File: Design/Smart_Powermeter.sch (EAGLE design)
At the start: 66 parts, among them IC1 AMS1117-3.3, IC3 ESP32-S2-MINI-1-N4R2, J1 AUDIO_JACK_TRRSSMD_RA, J2 AUDIO_JACK_TRRSSMD_RA, J3 AUDIO_JACK_TRRSSMD_RA, J4 AUDIO_JACK_TRRSSMD_RA, J5 AUDIO_JACK_TRRSSMD_RA, J6 AUDIO_JACK_TRRSSMD_RA, J8 USB-C, Q1 IRLML0100

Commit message: First draft for the Pro version
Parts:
- removed X1: (no value), con-wago-508:W237-02P
- added C16, C20, C21: 10u/6V, rcl:C-USC0603
- added D4, D5, D7: ESD5Z3.3T1G, microbuilder:DIODESOD-523
- added F1, F2, F3: 1A x 250V, OpenEnergyMonitor:FUSE
- added JP1, JP2, JP3, JP4, JP5, JP6: JUMPER-SMT_2_NC_TRACE_NO-SILK, SparkFun-Jumpers:JUMPER-SMT_2_NC_TRACE_NO-SILK
- added M1, M2, M3: 275VAC, OpenEnergyMonitor:MOV_14MM_275VAC
- added R21, R22, R23, R24, R26, R27, R28, R32, R33, R34, R35, R38, R39, R40, R48, R49, R50, R51, R52, R53, R54: 10k, rcl:R-US_R0603
- added R29, R41, R55: 180k, rcl:R-US_R0603
- added R30, R42, R56: 33k, rcl:R-US_R0603
- added R31, R43, R57: 1k, rcl:R-US_R0603
- added T1, T2, T3: ZMPT101B, OpenEnergyMonitor:ZMPT101B
- added X2: (no value), con-wago-508:W237-05P
- J1, J2, J3, J4, J5, J6: value AUDIO_JACK_TRRSSMD_RA -> AUDIO_JACK_MONO_3.5_3P; device SparkFun-Connectors:AUDIO_JACK_TRRSSMD_RA -> SpaceDIY_connectors:AUDIO_JACK_MONO_3.5_3P
- R10, R13, R16, R19, R4, R7: device rcl:R-US_R1206 -> rcl:R-US_R0603
- U$2: LCSC (none) -> C209909
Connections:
- removed net VG0: C1.1, J1.EARTH, R2.2, R3.1, R4.1
- new net L1: F1.2, M1.2, R48.1, U$2.AC_1
- new net L2: F2.2, M2.2, R21.1
- new net L3: F3.2, M3.2, R32.1
- new net N$10: R23.2, T2.PRI_1
- new net N$18: C20.1, R28.1, T2.SEC_2
- new net N$19: C20.2, R29.1, R30.2, R31.2
- new net N$20: R32.2, R33.1
- new net N$21: R33.2, R34.1
- new net N$22: R35.1, T3.PRI_2
- new net N$23: R35.2, R38.1
- new net N$24: R38.2, R39.1
- new net N$25: R48.2, R49.1
- new net N$26: R34.2, T3.PRI_1
- new net N$27: C21.1, R40.1, T3.SEC_2
- new net N$28: C21.2, R41.1, R42.2, R43.2
- new net N$29: JP2.2, R7.2
- new net N$3: F2.1, X2-2.KL
- new net N$30: JP3.2, R10.2
- new net N$33: JP4.2, R13.2
- new net N$34: JP5.2, R16.2
- new net N$35: JP6.2, R19.2
- new net N$36: R49.2, R50.1
- new net N$37: R51.1, T1.PRI_2
- new net N$38: R51.2, R52.1
- new net N$39: R52.2, R53.1
- new net N$4: F3.1, X2-3.KL
- new net N$40: R50.2, T1.PRI_1
- new net N$41: C16.1, R54.1, T1.SEC_2
- new net N$44: C16.2, R55.1, R56.2, R57.2
- new net N$5: R21.2, R22.1
- new net N$6: R22.2, R23.1
- new net N$7: R24.1, T2.PRI_2
- new net N$8: R24.2, R26.1
- new net N$9: R26.2, R27.1
- new net NEUTRAL: M1.1, M2.1, M3.1, R27.2, R39.2, R53.2, U$2.AC_2, X2-4.KL
- new net V1: D4.C, R57.1
- new net V2: D5.C, R31.1
- new net V3: D7.C, R43.1
- new net VG6: C6.1, J6.1, JP6.1, R17.2, R18.1
- net 3.3V: now also R29.2, R41.2, R55.2
- net GND: now also D4.A, D5.A, D7.A, R28.2, R30.1, R40.2, R42.1, R54.2, R56.1, T1.SEC_1, T2.SEC_1, T3.SEC_1, X2-5.KL
- net M1: now also J1.2, J1.3, R4.1; no longer J1.RING1, J1.RING2, J1.TIP, R4.2
- net M2: now also J2.2, J2.3, R7.1; no longer J2.RING1, J2.RING2, J2.TIP, R7.2
- net M3: now also J3.2, J3.3, R10.1; no longer J3.RING1, J3.RING2, J3.TIP, R10.2
- net M4: now also J4.2, J4.3, R13.1; no longer J4.RING1, J4.RING2, J4.TIP, R13.2
- net M5: now also J5.2, J5.3, R16.1; no longer J5.RING1, J5.RING2, J5.TIP, R16.2
- net M6: now also J6.2, J6.3, R19.1; no longer J6.RING1, J6.RING2, J6.TIP, R19.2
- net N$1: now also JP1.2, R4.2; no longer U$2.AC_2, X1-2.KL
- net N$2: now also F1.1, X2-1.KL; no longer U$2.AC_1, X1-1.KL
- net VG1: now also C1.1, J1.1, JP1.1, R2.2, R3.1; no longer C2.1, J2.EARTH, R5.2, R6.1, R7.1
- net VG2: now also C2.1, J2.1, JP2.1, R5.2, R6.1; no longer C3.1, J3.EARTH, R10.1, R8.2, R9.1
- net VG3: now also C3.1, J3.1, JP3.1, R8.2, R9.1; no longer C4.1, J4.EARTH, R11.2, R12.1, R13.1
- net VG4: now also C4.1, J4.1, JP4.1, R11.2, R12.1; no longer C5.1, J5.EARTH, R14.2, R15.1, R16.1
- net VG5: now also C5.1, J5.1, JP5.1, R14.2, R15.1; no longer C6.1, J6.EARTH, R17.2, R18.1, R19.1
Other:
- note added: "Voltage sensing"
- moved on the sheet: C11, C12, IC3, J7, J9, R10, R13, R16, R19, R4, R7

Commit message: Updated design files
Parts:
- added JP10, JP11, JP12, JP7, JP8, JP9: JUMPER-SMT_2_NO_NO-SILK, SparkFun-Jumpers:JUMPER-SMT_2_NO_NO-SILK
- added JP13: JUMPER-SMT_2_NC_PASTE_NO-SILK, SparkFun-Jumpers:JUMPER-SMT_2_NC_PASTE_NO-SILK
- added LED1: GREEN, SparkFun-LED:LED-GREEN0603
- added LED2: BLUE, SparkFun-LED:LED-BLUE0603
- added R44: 470, rcl:R-US_R0603
- added R45: 330, rcl:R-US_R0603
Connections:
- new net LED: IC3.IO8, R45.2
- new net N$42: LED1.A, R44.1
- new net N$43: JP13.2, R44.2
- new net N$45: LED2.A, R45.1
- new net N$46: J1.2, JP8.2
- new net N$47: J2.2, JP7.2
- new net N$48: J3.2, JP9.2
- new net N$49: J4.2, JP10.2
- new net N$50: J5.2, JP11.2
- new net N$51: J6.2, JP12.2
- net 3.3V: now also JP13.1
- net GND: now also LED1.C, LED2.C
- net M1: now also JP8.1; no longer J1.2
- net M2: now also JP7.1; no longer J2.2
- net M3: now also JP9.1; no longer J3.2
- net M4: now also JP10.1; no longer J4.2
- net M5: now also JP11.1; no longer J5.2
- net M6: now also JP12.1; no longer J6.2
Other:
- note added: "LED indicators"
- moved on the sheet: C10, C2, C20, C3, C4, C5, C6, C8, D5, IC1, R10, R11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

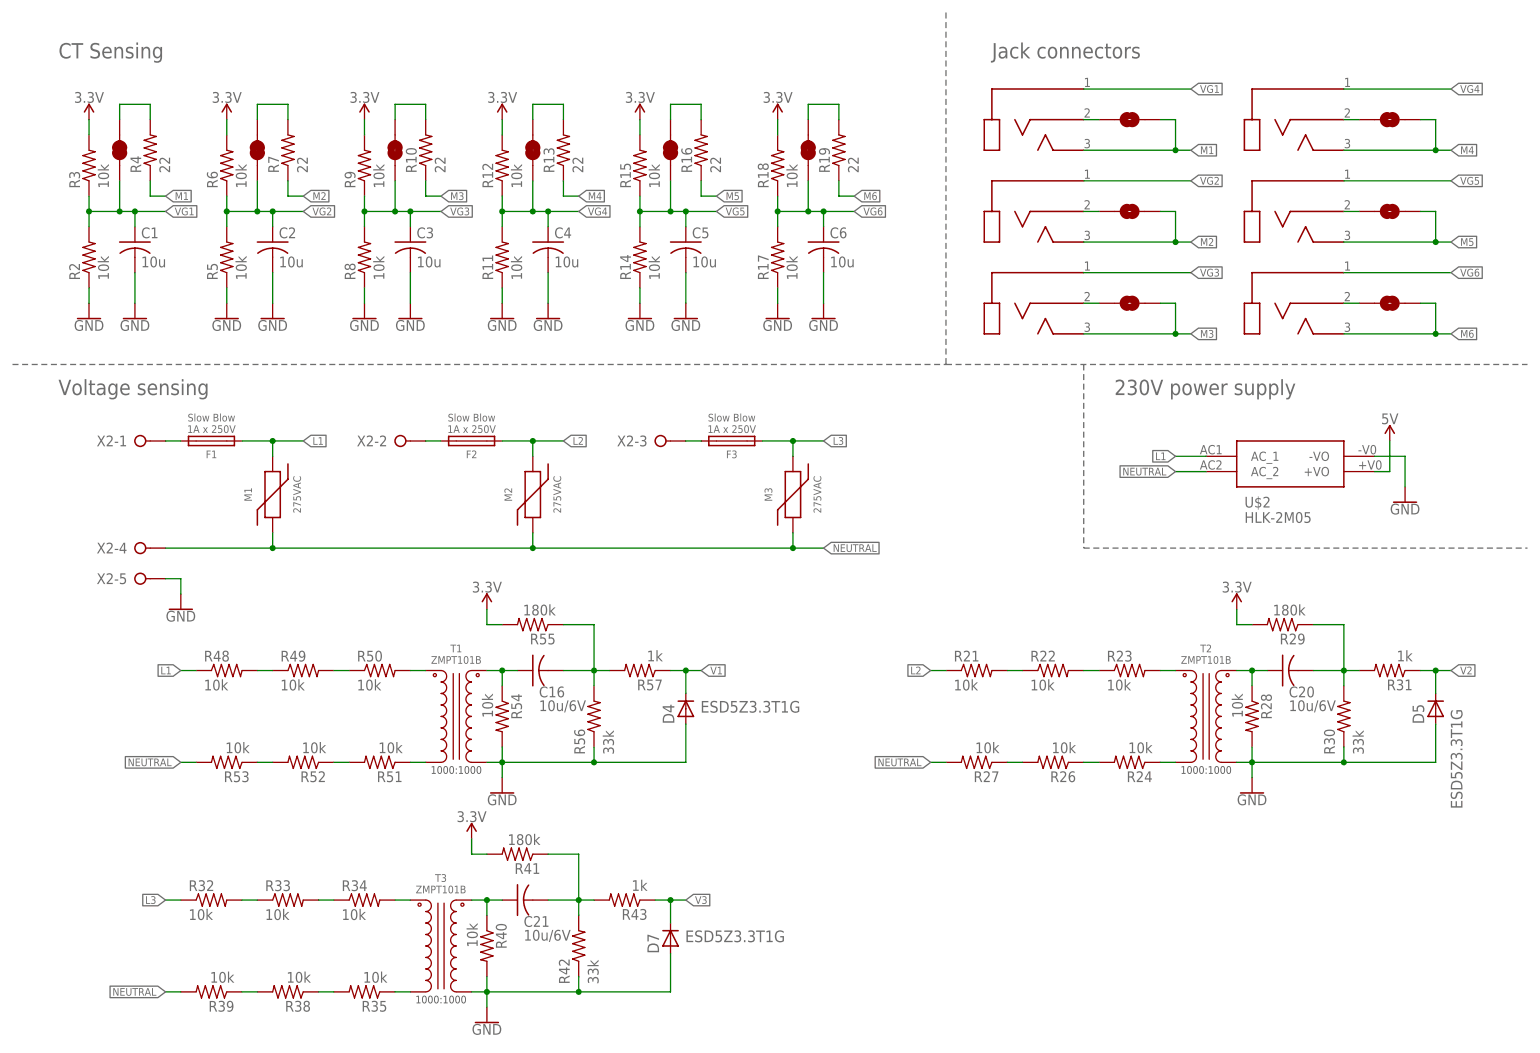
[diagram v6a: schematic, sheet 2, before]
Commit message: Smart Powermeter Pro with V/I measurements directly on the ESP32-S2
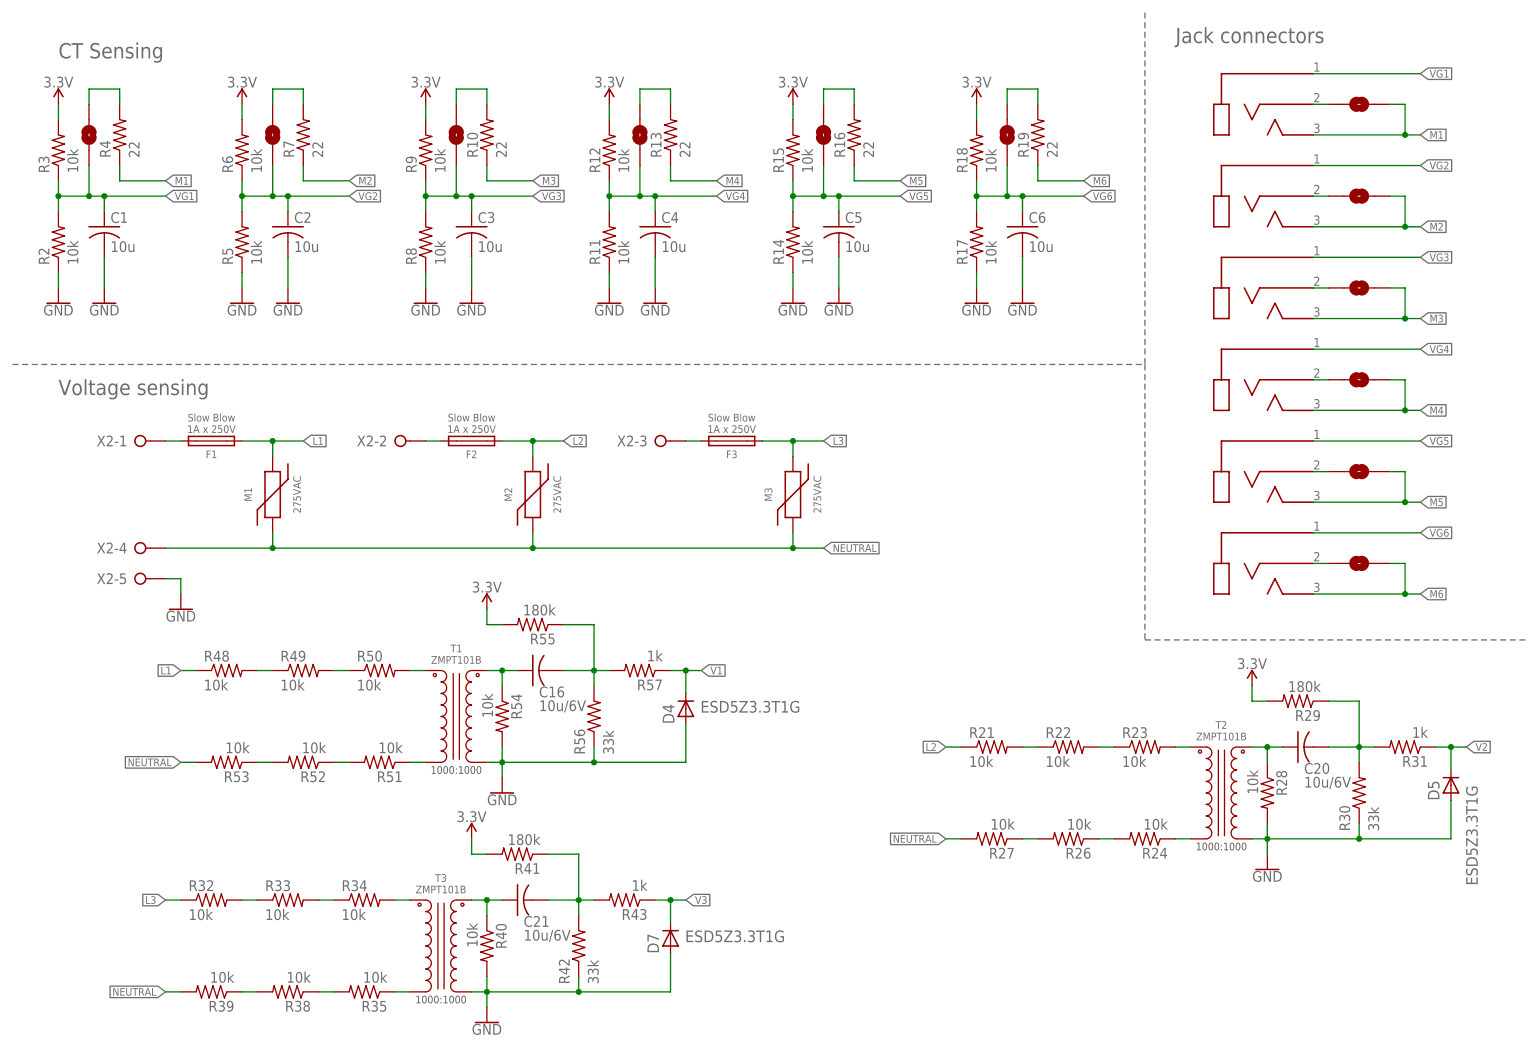
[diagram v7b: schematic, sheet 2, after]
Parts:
- JP1, JP2, JP3, JP4, JP5, JP6: value JUMPER-SMT_2_NC_TRACE_NO-SILK -> JUMPER-SMT_2_NO_NO-SILK; device SparkFun-Jumpers:JUMPER-SMT_2_NC_TRACE_NO-SILK -> SparkFun-Jumpers:JUMPER-SMT_2_NO_NO-SILK
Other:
- moved on the sheet: C1, C10, C2, C20, C3, C4, C5, C6, C8, D5, IC1, JP13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
